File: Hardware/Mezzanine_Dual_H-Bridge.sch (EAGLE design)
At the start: 25 parts, among them U1 TB6612FNG, U2 EDISON_CONNECTOR_FULLMOUNTING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, U3 EDISON_CONNECTOR_FULLHEADER

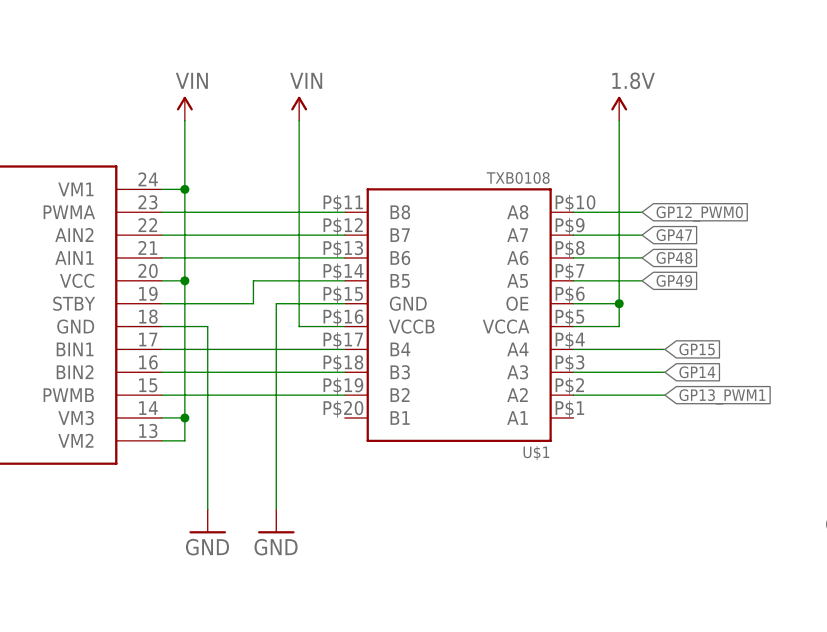
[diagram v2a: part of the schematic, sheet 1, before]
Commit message: corrected labels
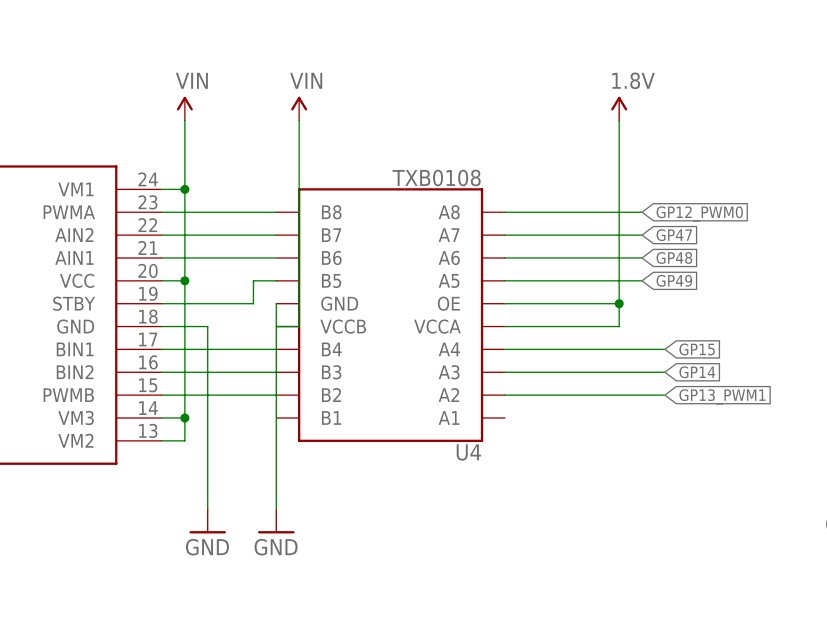
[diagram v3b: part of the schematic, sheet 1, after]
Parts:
- removed U$1: TXB0108, Testing:TXB0108
- added U4: TXB0108, Testing:TXB0108
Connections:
- net 1.8V: now also U4.OE, U4.VCCA; no longer U$1.OE, U$1.VCCA
- net GND: now also U4.GND; no longer U$1.GND
- net GP12_PWM0: now also U4.A8; no longer U$1.A8
- net GP13_PWM1: now also U4.A2; no longer U$1.A2
- net GP14: now also U4.A3; no longer U$1.A3
- net GP15: now also U4.A4; no longer U$1.A4
- net GP47: now also U4.A7; no longer U$1.A7
- net GP48: now also U4.A6; no longer U$1.A6
- net GP49: now also U4.A5; no longer U$1.A5
- net N$10: now also U4.B5; no longer U$1.B5
- net N$11: now also U4.B4; no longer U$1.B4
- net N$12: now also U4.B3; no longer U$1.B3
- net N$14: now also U4.B6; no longer U$1.B6
- net N$15: now also U4.B7; no longer U$1.B7
- net N$3: now also U4.B2; no longer U$1.B2
- net N$4: now also U4.B8; no longer U$1.B8
- net VIN: now also U4.VCCB; no longer U$1.VCCB
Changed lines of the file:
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@@
 <part name="SUPPLY1" library="SparkFun-Aesthetics" deviceset="VIN" device=""/>
 <part name="SUPPLY2" library="SparkFun-Aesthetics" deviceset="VIN" device=""/>
-<part name="U$1" library="Testing" deviceset="TXB0108" device=""/>
+<part name="U4" library="Testing" deviceset="TXB0108" device=""/>
 <part name="GND6" library="SparkFun-Aesthetics" deviceset="GND" device=""/>
 <part name="SUPPLY3" library="SparkFun-Aesthetics" deviceset="VIN" device=""/>
@@
 <instance part="SUPPLY1" gate="G$1" x="40.64" y="129.54"/>
 <instance part="SUPPLY2" gate="G$1" x="137.16" y="129.54"/>
-<instance part="U$1" gate="G$1" x="160.02" y="106.68" rot="R180"/>
+<instance part="U4" gate="U1" x="160.02" y="106.68" rot="R180"/>
 <instance part="GND6" gate="1" x="147.32" y="83.82"/>
 <instance part="SUPPLY3" gate="G$1" x="149.86" y="129.54"/>
@@
 </segment>
 <segment>
-<wire x1="154.94" y1="109.22" x2="147.32" y2="109.22" width="0.1524" layer="91"/>
 <wire x1="147.32" y1="109.22" x2="147.32" y2="86.36" width="0.1524" layer="91"/>
 <pinref part="GND6" gate="1" pin="GND"/>
-<pinref part="U$1" gate="G$1" pin="GND"/>
+<pinref part="U4" gate="U1" pin="GND"/>
 </segment>
 <segment>
@@
 <wire x1="134.62" y1="109.22" x2="144.78" y2="109.22" width="0.1524" layer="91"/>
 <wire x1="144.78" y1="109.22" x2="144.78" y2="111.76" width="0.1524" layer="91"/>
-<wire x1="144.78" y1="111.76" x2="154.94" y2="111.76" width="0.1524" layer="91"/>
-<pinref part="U$1" gate="G$1" pin="B5"/>
+<wire x1="144.78" y1="111.76" x2="147.32" y2="111.76" width="0.1524" layer="91"/>
+<pinref part="U4" gate="U1" pin="B5"/>
 </segment>
 </net>
@@
 <segment>
 <pinref part="U1" gate="G$1" pin="BIN1"/>
-<wire x1="134.62" y1="104.14" x2="154.94" y2="104.14" width="0.1524" layer="91"/>
-<pinref part="U$1" gate="G$1" pin="B4"/>
+<wire x1="134.62" y1="104.14" x2="147.32" y2="104.14" width="0.1524" layer="91"/>
+<pinref part="U4" gate="U1" pin="B4"/>
 </segment>
 </net>
@@
 <segment>
 <pinref part="U1" gate="G$1" pin="BIN2"/>
-<wire x1="134.62" y1="101.6" x2="154.94" y2="101.6" width="0.1524" layer="91"/>
-<pinref part="U$1" gate="G$1" pin="B3"/>
+<wire x1="134.62" y1="101.6" x2="147.32" y2="101.6" width="0.1524" layer="91"/>
+<pinref part="U4" gate="U1" pin="B3"/>
 </segment>
 </net>
@@
 <segment>
 <pinref part="U1" gate="G$1" pin="AIN1"/>
-<wire x1="154.94" y1="114.3" x2="134.62" y2="114.3" width="0.1524" layer="91"/>
-<pinref part="U$1" gate="G$1" pin="B6"/>
+<wire x1="147.32" y1="114.3" x2="134.62" y2="114.3" width="0.1524" layer="91"/>
+<pinref part="U4" gate="U1" pin="B6"/>
 </segment>
 </net>
@@
 <segment>
 <pinref part="U1" gate="G$1" pin="AIN2"/>
-<wire x1="134.62" y1="116.84" x2="154.94" y2="116.84" width="0.1524" layer="91"/>
-<pinref part="U$1" gate="G$1" pin="B7"/>
+<wire x1="134.62" y1="116.84" x2="147.32" y2="116.84" width="0.1524" layer="91"/>
+<pinref part="U4" gate="U1" pin="B7"/>
 </segment>
 </net>
@@
 </segment>
 <segment>
-<wire x1="154.94" y1="106.68" x2="149.86" y2="106.68" width="0.1524" layer="91"/>
+<wire x1="147.32" y1="106.68" x2="149.86" y2="106.68" width="0.1524" layer="91"/>
 <wire x1="149.86" y1="106.68" x2="149.86" y2="129.54" width="0.1524" layer="91"/>
 <pinref part="SUPPLY3" gate="G$1" pin="VIN"/>
-<pinref part="U$1" gate="G$1" pin="VCCB"/>
+<pinref part="U4" gate="U1" pin="VCCB"/>
 </segment>
 <segment>
@@
 <segment>
 <pinref part="U1" gate="G$1" pin="PWMB"/>
-<wire x1="134.62" y1="99.06" x2="154.94" y2="99.06" width="0.1524" layer="91"/>
-<pinref part="U$1" gate="G$1" pin="B2"/>
+<wire x1="134.62" y1="99.06" x2="147.32" y2="99.06" width="0.1524" layer="91"/>
+<pinref part="U4" gate="U1" pin="B2"/>
 </segment>
 </net>
@@
 <segment>
 <pinref part="U1" gate="G$1" pin="PWMA"/>
-<wire x1="134.62" y1="119.38" x2="154.94" y2="119.38" width="0.1524" layer="91"/>
-<pinref part="U$1" gate="G$1" pin="B8"/>
+<wire x1="134.62" y1="119.38" x2="147.32" y2="119.38" width="0.1524" layer="91"/>
+<pinref part="U4" gate="U1" pin="B8"/>
 </segment>
 </net>
 <net name="1.8V" class="0">
 <segment>
-<wire x1="180.34" y1="106.68" x2="185.42" y2="106.68" width="0.1524" layer="91"/>
+<wire x1="172.72" y1="106.68" x2="185.42" y2="106.68" width="0.1524" layer="91"/>
 <wire x1="185.42" y1="106.68" x2="185.42" y2="109.22" width="0.1524" layer="91"/>
 <pinref part="SUPPLY4" gate="G$1" pin="1.8V"/>
-<pinref part="U$1" gate="G$1" pin="VCCA"/>
-<pinref part="U$1" gate="G$1" pin="OE"/>
+<pinref part="U4" gate="U1" pin="VCCA"/>
+<pinref part="U4" gate="U1" pin="OE"/>
 <wire x1="185.42" y1="109.22" x2="185.42" y2="129.54" width="0.1524" layer="91"/>
-<wire x1="180.34" y1="109.22" x2="185.42" y2="109.22" width="0.1524" layer="91"/>
+<wire x1="172.72" y1="109.22" x2="185.42" y2="109.22" width="0.1524" layer="91"/>
 <junction x="185.42" y="109.22"/>
 </segment>
@@
 <segment>
 <label x="190.5" y="99.06" size="1.27" layer="95" rot="MR180" xref="yes"/>
-<wire x1="180.34" y1="99.06" x2="190.5" y2="99.06" width="0.1524" layer="91"/>
-<pinref part="U$1" gate="G$1" pin="A2"/>
+<wire x1="172.72" y1="99.06" x2="190.5" y2="99.06" width="0.1524" layer="91"/>
+<pinref part="U4" gate="U1" pin="A2"/>
 </segment>
 </net>
@@
 <segment>
 <label x="187.96" y="119.38" size="1.27" layer="95" rot="MR180" xref="yes"/>
-<wire x1="180.34" y1="119.38" x2="187.96" y2="119.38" width="0.1524" layer="91"/>
-<pinref part="U$1" gate="G$1" pin="A8"/>
+<wire x1="172.72" y1="119.38" x2="187.96" y2="119.38" width="0.1524" layer="91"/>
+<pinref part="U4" gate="U1" pin="A8"/>
 </segment>
 </net>
@@
 <segment>
 <label x="190.5" y="101.6" size="1.27" layer="95" rot="MR180" xref="yes"/>
-<wire x1="180.34" y1="101.6" x2="190.5" y2="101.6" width="0.1524" layer="91"/>
-<pinref part="U$1" gate="G$1" pin="A3"/>
+<wire x1="172.72" y1="101.6" x2="190.5" y2="101.6" width="0.1524" layer="91"/>
+<pinref part="U4" gate="U1" pin="A3"/>
 </segment>
 </net>
@@
 <segment>
 <label x="190.5" y="104.14" size="1.27" layer="95" rot="MR180" xref="yes"/>
-<wire x1="180.34" y1="104.14" x2="190.5" y2="104.14" width="0.1524" layer="91"/>
-<pinref part="U$1" gate="G$1" pin="A4"/>
+<wire x1="172.72" y1="104.14" x2="190.5" y2="104.14" width="0.1524" layer="91"/>
+<pinref part="U4" gate="U1" pin="A4"/>
 </segment>
 </net>
@@
 <segment>
 <label x="187.96" y="111.76" size="1.27" layer="95" rot="MR180" xref="yes"/>
-<wire x1="180.34" y1="111.76" x2="187.96" y2="111.76" width="0.1524" layer="91"/>
-<pinref part="U$1" gate="G$1" pin="A5"/>
+<wire x1="172.72" y1="111.76" x2="187.96" y2="111.76" width="0.1524" layer="91"/>
+<pinref part="U4" gate="U1" pin="A5"/>
 </segment>
 </net>
@@
 <segment>
 <label x="187.96" y="114.3" size="1.27" layer="95" rot="MR180" xref="yes"/>
-<wire x1="180.34" y1="114.3" x2="187.96" y2="114.3" width="0.1524" layer="91"/>
-<pinref part="U$1" gate="G$1" pin="A6"/>
+<wire x1="172.72" y1="114.3" x2="187.96" y2="114.3" width="0.1524" layer="91"/>
+<pinref part="U4" gate="U1" pin="A6"/>
 </segment>
 </net>
@@
 <segment>
 <label x="187.96" y="116.84" size="1.27" layer="95" rot="MR180" xref="yes"/>
-<wire x1="180.34" y1="116.84" x2="187.96" y2="116.84" width="0.1524" layer="91"/>
-<pinref part="U$1" gate="G$1" pin="A7"/>
-</segment>
-</net>
+<wire x1="172.72" y1="116.84" x2="187.96" y2="116.84" width="0.1524" layer="91"/>
+<pinref part="U4" gate="U1" pin="A7"/>
+</segment>
+</net>
